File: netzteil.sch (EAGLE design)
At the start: 61 parts, among them IC1 LM723N, IC2 TL072P, Q1 BC559A, X1 MKDSN1,5/3-5,08, X10 2N3055, X11 MKDSN1,5/3-5,08, X12 POWER_KO, X13 V+, X14 V-, X2 MKDSN1,5/2-5,08, X3 MKDSN1,5/2-5,08, X4 50k, X5 1k, X7 STROMMESSUNG, X8 2N3055, X9 2N3055

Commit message: added minimum temperature enable for fan, fixed errors in regulation, adapted clamps for panel meters, added C.V. and overtemperature display diode, seperate supply for fan
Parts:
- removed X12: POWER_KO, con-phoenix-508:MKDSN1,5/2-5,08
- added B1, B2: (no value), rectifier:2KBB
- added C12, C13: 100n, rcl:C-EU025-025X050
- added C14: 10u, rcl:CPOL-EUE3.5-8
- added C4, C5: 2200u/63V, rcl:CPOL-EUE7.5-18
- added D10, D12, D9: 1N4148DO35-7, diode:1N4148DO35-7
- added D11, D13: 3v3, diode:ZENER-DIODEDO34-7
- added D8: 1N4004, adafruit:1N4004
- added IC3: TL084P, linear:TL084P
- added IC4: UA741P, linear:UA741P
- added LED2, LED3: (no value), adafruit:LED3MM
- added Q2, Q3, Q4: BC559A, transistor-pnp:BC559A
- added R27, R29, R30, R40: 0R22/4W, powerR:R
- added R28, R36: 100k, rcl:R-TRIMM3296Y
- added R31: 10R, rcl:R-EU_0207/2V
- added R32, R33, R35, R37, R38: 4k7, rcl:R-EU_0207/2V
- added R34, R39: 470R/1W, rcl:R-EU_0207/2V
- added T2: BD241, transistor:-NPN-TO220V
- added T3, T4, T5, T6: BD243, transistor:BD243
- added X6: VPOWER, con-phoenix-508:MKDSN1,5/2-5,08
- C10: value 100p -> 56p
- D6: value (none) -> 3v3
- IC2: value TL072P -> UA741P; device linear:TL072P -> linear:UA741P
- R12: device rcl:R-EU_0411/12 -> rcl:R-EU_0207/10
- R13: value R22/3W -> 0R22/4W; device rcl:R-EU_0411/12 -> powerR:R
- R16: value 10R/1W -> 100k; device rcl:R-EU_0411/12 -> rcl:R-TRIMM3296Y
- R17: value R22/3W -> 2k2; device rcl:R-EU_0411/12 -> rcl:R-EU_0207/2V
- R18: value R22/3W -> 560R; device rcl:R-EU_0411/12 -> rcl:R-EU_0207/2V
- R19: value R22/3W -> 4k7; device rcl:R-EU_0411/12 -> rcl:R-EU_0207/7
- R24: value 470k -> 4k7
- R25: value 10k -> 0R22/4W; device rcl:R-TRIMM3296Y -> powerR:R
- R26: value 10k -> 4k7
- T1: value (none) -> BD243; device transistor-neu-to92:-NPN-TO220 -> transistor:BD243
- X10: value 2N3055 -> FAN; device con-phoenix-508:MKDSN1,5/3-5,08 -> con-phoenix-508:MKDSN1,5/2-5,08
- X11: value MKDSN1,5/3-5,08 -> SHUNT; device con-phoenix-508:MKDSN1,5/3-5,08 -> con-phoenix-508:MKDSN1,5/2-5,08
- X2: value MKDSN1,5/2-5,08 -> Vmess
- X3: value MKDSN1,5/2-5,08 -> OUTPUTCAP
- X7: value STROMMESSUNG -> VFAN
- X9: value 2N3055 -> NTC; device con-phoenix-508:MKDSN1,5/3-5,08 -> nxs_con-misc:PCB2_TERMINAL-BLOCK
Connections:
- new net N$30: R23.2, R6.1, X14-1.KL, X4-1.KL
- new net N$33: D10.C, R26.E, R32.2
- new net N$34: LED2.A, R34.1
- new net N$35: C16.+, X3-2.KL
- new net N$36: D12.C, IC3A.OUT, Q3.E
- new net N$37: Q3.C, R18.2
- new net N$38: D12.A, Q3.B, R35.1
- new net N$39: IC3C.OUT, R35.2
- new net N$40: IC3C.+IN, R36.S
- new net N$41: IC3A.-IN, R16.S
- new net N$42: C12.1, IC3B.-IN, R19.1
- new net N$43: IC3D.-IN, IC3D.OUT
- new net N$44: R18.1, T1.B
- new net N$45: IC3B.+IN, R28.S
- new net N$46: D8.C, R16.A, T1.E, X10-1.KL
- new net N$47: C12.2, D9.C, IC3B.OUT, R37.2
- new net N$48: R17.2, R19.2, X9-2.KL
- new net N$49: R31.2, T2.E, T3.B, T4.B, T5.B, T6.B
- new net N$50: R27.P$1, T3.E
- new net N$51: R29.P$1, T4.E
- new net N$52: R30.P$1, T5.E
- new net N$53: B2.AC1, X7-2.KL
- new net N$54: B2.AC2, X7-1.KL
- new net N$55: B2.+, C14.+, T1.C
- new net N$56: D13.C, Q4.B, R38.2
- new net N$57: D13.A, R37.1
- new net N$58: Q4.C, R39.2
- new net N$59: LED3.A, R39.1
- new net N$63: R40.P$1, T6.E
- net AGND: now also C4.-, C5.+, D10.A, IC3D.+IN, LED2.C, LED3.C, R7.1; no longer C8.2, C9.1, R6.1, X2-2.KL, X3-1.KL, X4-1.KL, X5-1.KL
- net N$10: now also IC2.OUT, R24.2; no longer IC2A.OUT
- net N$11: now also IC4.-IN; no longer IC2B.-IN
- net N$12: now also IC4.+IN; no longer IC2B.+IN
- net N$15: now also D9.A, T2.B, X8-2.KL; no longer T1.B
- net N$16: now also IC4.OUT; no longer IC2B.OUT
- net N$17: now also R13.P$1, R27.P$2, R29.P$2, R30.P$2, R31.1, R40.P$2, X11-1.KL, X8-3.KL; no longer R13.2, R16.1, R17.1, R18.1, R19.1, R25.A
- net N$18: now also R25.P$2, X2-1.KL, X3-1.KL; no longer C16.+, R13.1, R24.1, R25.E, X7-1.KL
- net N$19: now also R13.P$2, R25.P$1, X11-2.KL; no longer R25.S, X7-2.KL
- net N$21: now also D11.C, Q2.B, R33.2; no longer R16.2, T1.E, X10-2.KL, X8-2.KL, X9-2.KL
- net N$22: now also D11.A, R24.1; no longer R17.2, X10-3.KL
- net N$23: now also B1.AC1, X1-3.KL; no longer R18.2, X9-3.KL
- net N$24: now also B1.AC2, X1-1.KL; no longer R19.2, X8-3.KL
- net N$25: now also Q2.C, R34.2; no longer R24.2, R26.E, R26.S
- net N$29: now also T2.C, T3.C, T4.C, T5.C, T6.C, X6-2.KL; no longer T1.C, X10-1.KL, X11-3.KL, X12-2.KL, X9-1.KL
- net N$3: now also IC2.+IN; no longer IC2A.+IN
- net N$31: now also X2-2.KL, X6-1.KL; no longer R26.A, X11-1.KL, X12-1.KL
- net N$32: now also R26.S, X5-1.KL; no longer R23.2, R7.1, X14-1.KL
- net N$8: now also IC2.-IN; no longer IC2A.-IN
- net V+: now also B1.+, C13.1, C4.+, C9.1, IC2.V+, IC3A.+IN, IC3C.-IN, IC3P.V+, IC4.V+, Q2.E, Q4.E, R28.E, R33.1, R36.E, R38.1, X9-1.KL; no longer IC2P.V+, X1-3.KL, X3-2.KL
- net V-: now also B1.-, B2.-, C13.2, C14.-, C5.-, C8.2, D8.A, IC2.V-, IC3P.V-, IC4.V-, R16.E, R17.1, R28.A, R32.1, R36.A, X10-2.KL; no longer IC2P.V-, X1-1.KL, X2-1.KL
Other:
- note added: "SENSE+"
- note added: "SENSE-"
- note added: "V4"
- moved on the sheet: C10, C11, C16, C7, C8, C9, D5, D6, D7, LED1, Q1, R10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

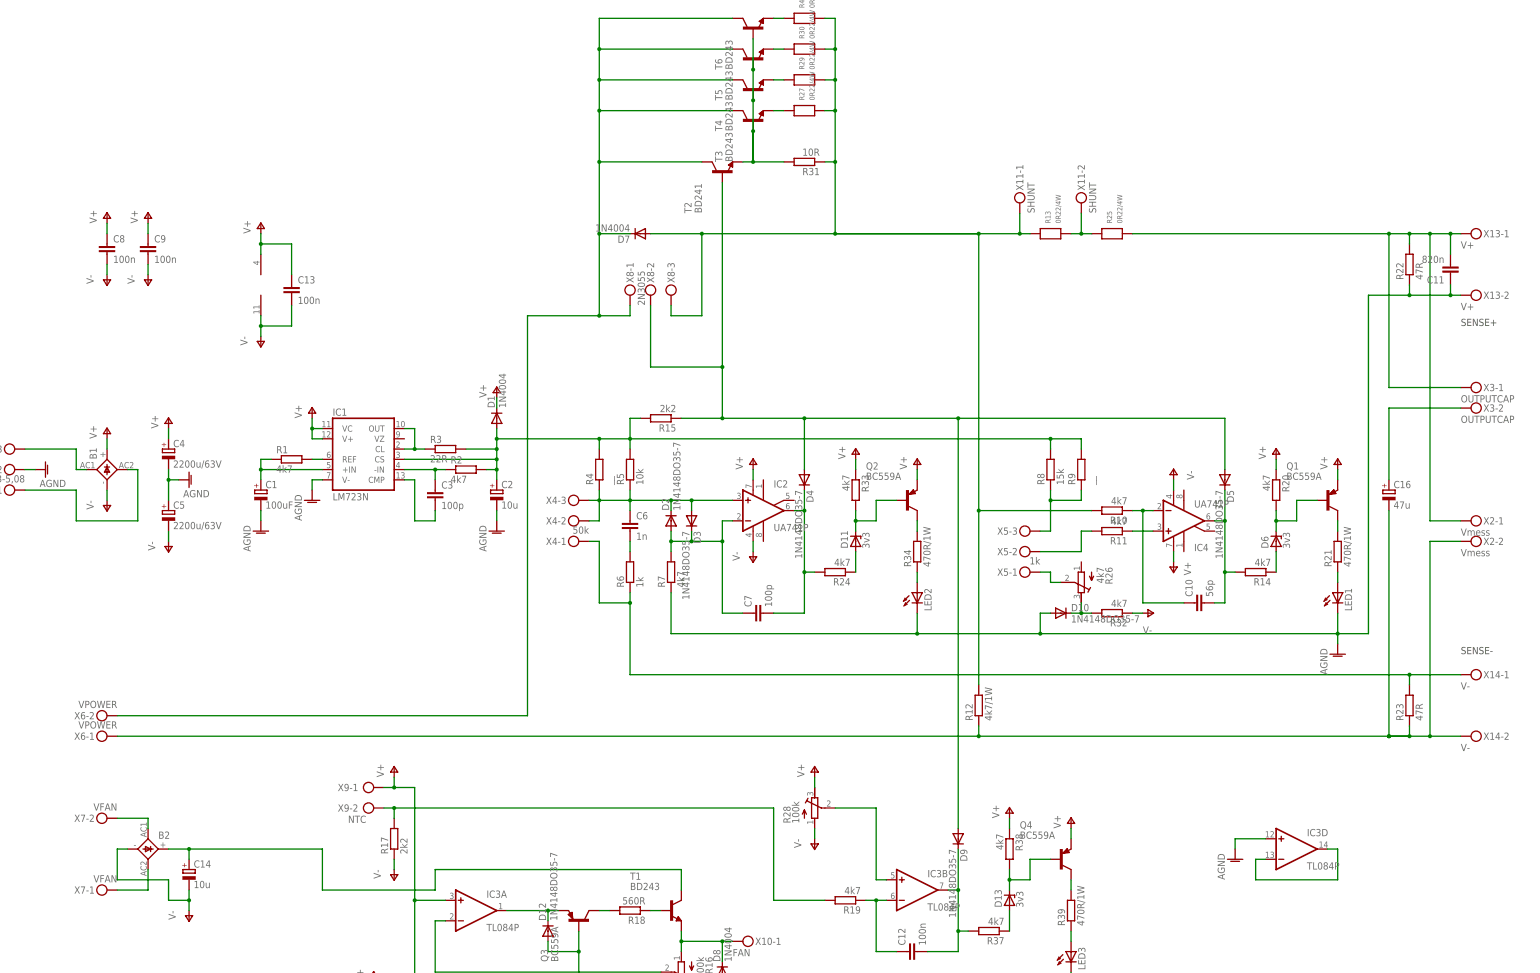
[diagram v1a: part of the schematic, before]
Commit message: added amperemeter and shunt clamps, semi-final version of the schematic for the pcb
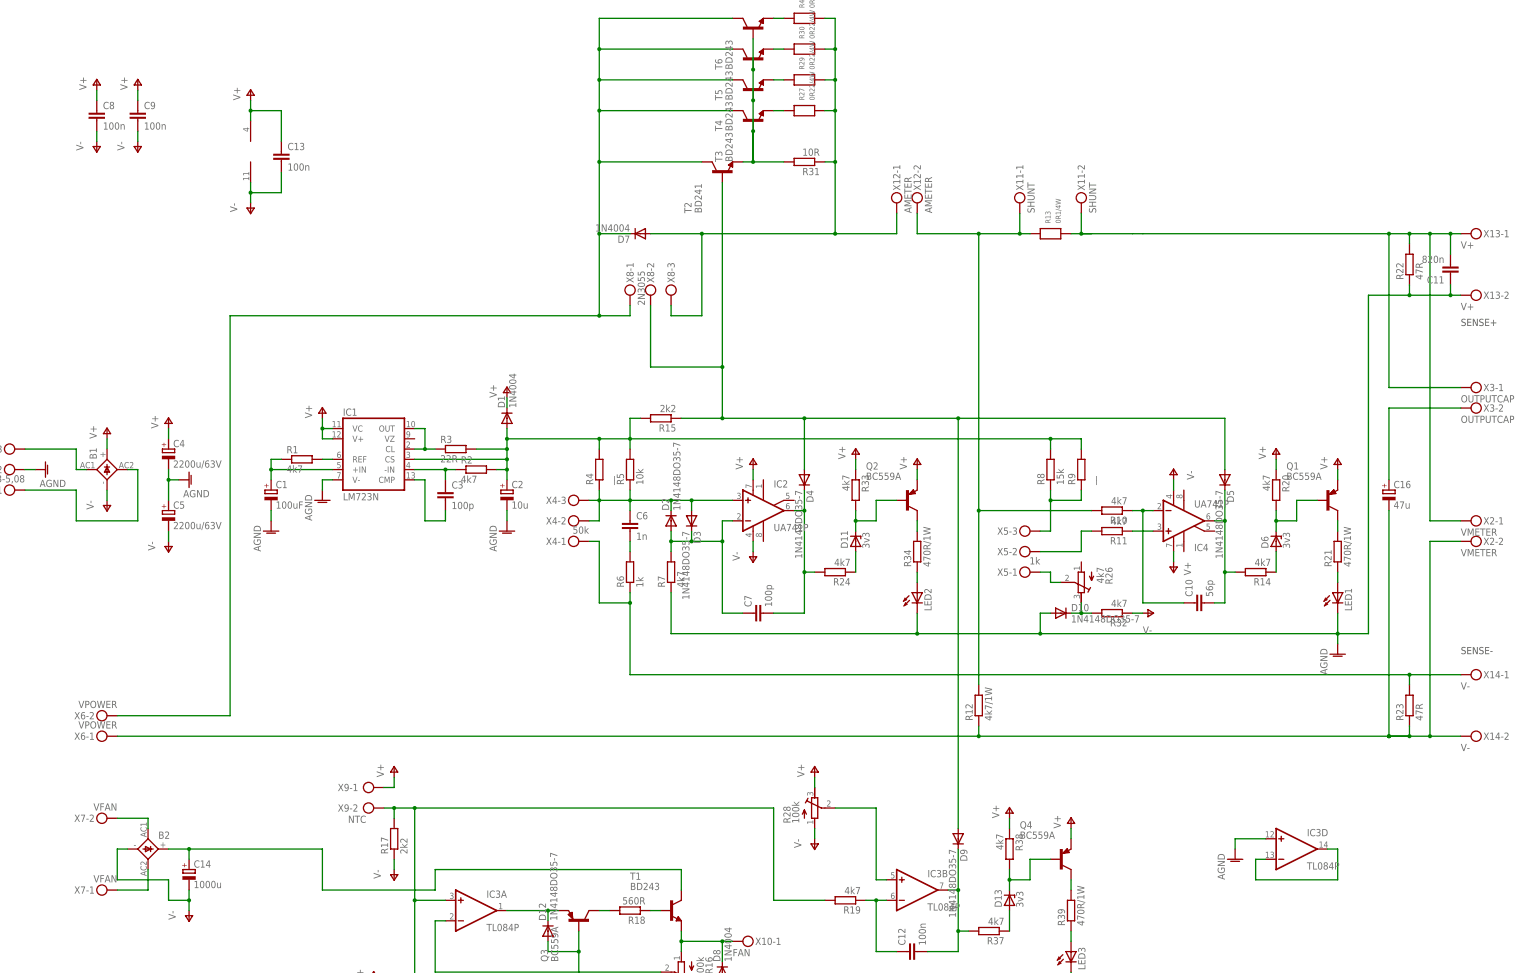
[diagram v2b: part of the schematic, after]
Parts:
- removed R25: 0R22/4W, powerR:R
- added X12: AMETER, con-phoenix-508:MKDSN1,5/2-5,08
- C14: value 10u -> 1000u
- R13: value 0R22/4W -> 0R1/4W
- X2: value Vmess -> VMETER
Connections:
- net N$17: now also X12-2.KL; no longer D7.A, R27.P$2, R29.P$2, R30.P$2, R31.1, R40.P$2, X8-3.KL
- net N$18: now also R13.P$2, X11-2.KL; no longer R25.P$2
- net N$19: now also D7.A, R27.P$2, R29.P$2, R30.P$2, R31.1, R40.P$2, X12-1.KL, X8-3.KL; no longer R13.P$2, R25.P$1, X11-2.KL
- net N$48: now also IC3A.+IN, IC3C.-IN
- net V+: no longer IC3A.+IN, IC3C.-IN
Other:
- moved on the sheet: C1, C13, C2, C3, C8, C9, D1, IC1, R1, R2, R3

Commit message: finished pre-final pcb layout
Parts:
- added C15: 100n, rcl:C-EU025-025X050
- B1, B2: device rectifier:2KBB -> rectifier:1KAB
- C14: value 1000u -> 470u; device rcl:CPOL-EUE3.5-8 -> rcl:CPOL-EUE5-13
- C4, C5: value 2200u/63V -> 1000u/63V
- D1: device adafruit:1N4004 -> diode:1N4004
- D11, D13, D6: device diode:ZENER-DIODEDO34-7 -> diode:ZENER-DIODE
- D12, D2, D3: value 1N4148DO35-7 -> 1N4148V; device diode:1N4148DO35-7 -> diode:1N4148V
- X1: value MKDSN1,5/3-5,08 -> VCONTROL
- X9: device nxs_con-misc:PCB2_TERMINAL-BLOCK -> con-phoenix-508:MKDSN1,5/2-5,08
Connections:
- net N$7 renamed V723
- net AGND: now also IC3A.+IN; no longer IC3D.+IN
- net N$36: now also IC3D.OUT; no longer IC3A.OUT
- net N$41: now also IC3D.-IN; no longer IC3A.-IN
- net N$43: now also IC3A.-IN, IC3A.OUT; no longer IC3D.-IN, IC3D.OUT
- net N$48: now also C15.1, IC3D.+IN, X9-1.KL; no longer IC3A.+IN, X9-2.KL
- net V+: now also X9-2.KL; no longer X9-1.KL
- net V-: now also C15.2
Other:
- moved on the sheet: IC3A, IC3D, X9-1, X9-2

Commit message: moved mechanical to thingiverse
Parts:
- removed D10: 1N4148DO35-7, diode:1N4148DO35-7
- removed R32: 4k7, rcl:R-EU_0207/2V
- added F1: FUSEPICOFUSE, fuse:FUSEPICOFUSE
- added F2: 50mA, fuse:FUSEPICOFUSE
- added R25: 1k, rcl:R-EU_0207/2V
- added R41: 10k, rcl:R-EU_0207/2V
- added TP1, TP2, TP3, TP4, TP5: TPPAD1-13, testpad:TPPAD1-13
- T1, T3, T4, T5, T6: device transistor:BD243 -> transistor:-NPN-TO220V
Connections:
- new net N$60: F1.1, X13-2.KL
- new net N$7: IC3A.-IN, R25.2, R41.2
- net AGND: now also F1.2, TP2.TP; no longer D10.A, X13-2.KL
- net N$15: now also TP3.TP
- net N$30: now also F2.1; no longer X14-1.KL
- net N$33: now also IC3A.OUT, R25.1; no longer D10.C, R32.2
- net N$43: now also F2.2, X14-1.KL; no longer IC3A.-IN, IC3A.OUT
- net V+: now also TP5.TP
- net V-: now also TP4.TP; no longer R32.1
- net V723: now also R41.1, TP1.TP
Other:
- moved on the sheet: B1, C13, C4, C5, C8, C9, D13, D6, IC3A, R14, R20, R37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

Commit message: update readme.md
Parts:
- F1: value FUSEPICOFUSE -> 50mA
